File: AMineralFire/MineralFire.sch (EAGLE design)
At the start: 77 parts, among them IC1 LM358, IC2 OP-AMP, Q1 20MHz, Q2 20MHz, Q3 2N3906, Q4 2N3906, Q5 2N3906, Q6 2N3906, Q7 2N3906, Q8 2N3906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

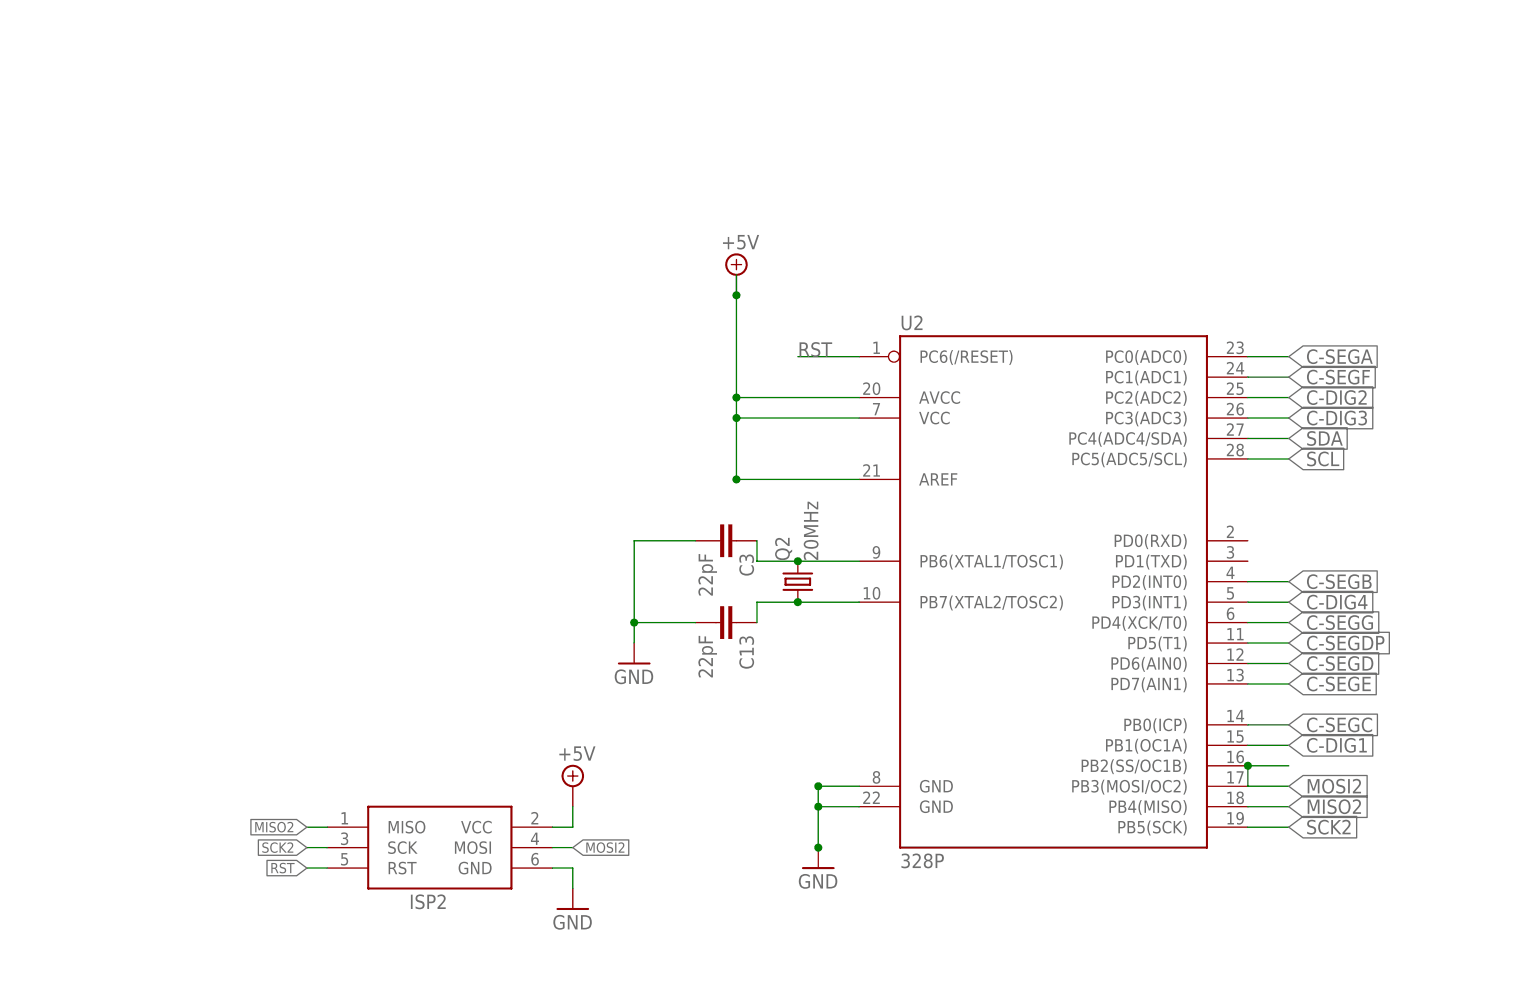
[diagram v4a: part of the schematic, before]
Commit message: Moving atmega to smd
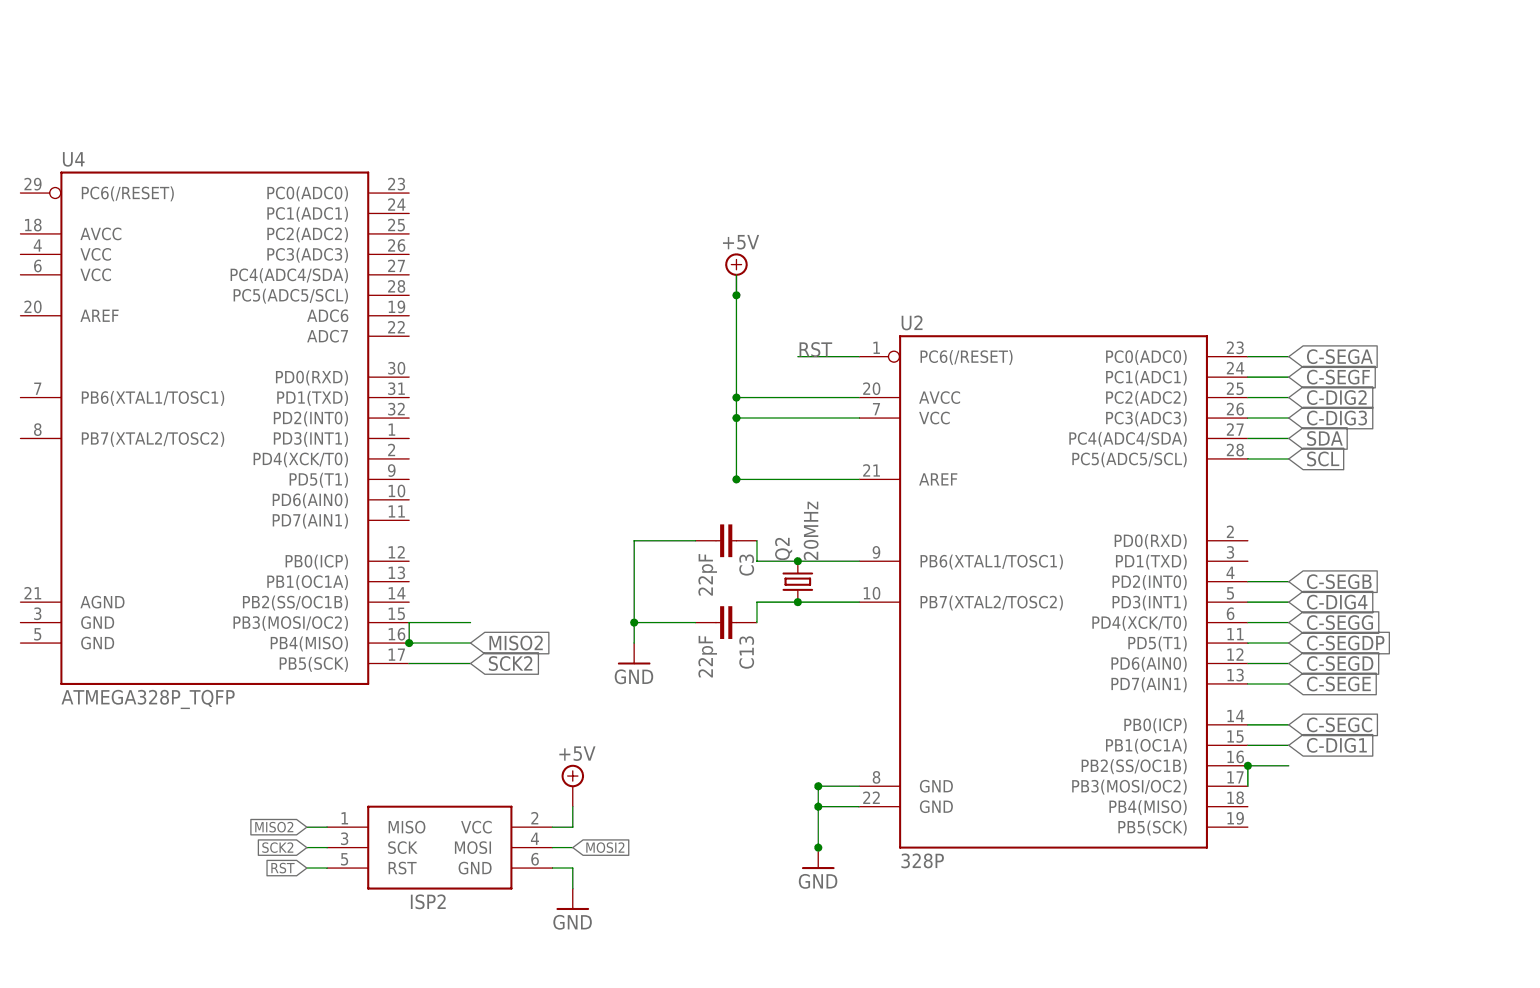
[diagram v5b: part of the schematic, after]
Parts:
- added U4: ATMEGA328P_TQFP, SparkFun-IC-Microcontroller:ATMEGA328P_TQFP
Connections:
- net MISO2: now also U4.PB3(MOSI/OC2), U4.PB4(MISO); no longer U2.PB4(MISO)
- net SCK2: now also U4.PB5(SCK); no longer U2.PB5(SCK)

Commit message: moving to SMD
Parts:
- removed C1, C2: 22pF, SparkFun-Capacitors:22PF-0603-50V-5%
- removed IC1: LM358, SparkFun-IC-Amplifiers:LM358
- removed Q1: 20MHz, adafruit:CRYSTALHC49UP
- removed U1, U2: 328P, SparkFun-IC-Microcontroller:ATMEGA328P_PDIP
- removed V1: 7432N, 74ttl-din:7432N
- added C14, C15: 22pF, SparkFun-Capacitors:22PF-0603-50V-5%
- added IC3: 7432D, 74xx-us:7432D
- added Q10: 20MHz, adafruit:CRYSTALHC49UP
- added U5: ATMEGA328P_TQFP, SparkFun-IC-Microcontroller:ATMEGA328P_TQFP
- C6: device rcl:C-EU075-032X103 -> rcl:C-EU01005
- D1, D2: value 200mA/100V/1V -> 250mA/100V; device SparkFun-DiscreteSemi:DIODE-1N4148 -> SparkFun-DiscreteSemi:DIODE-BAS16J
- Q3, Q4, Q5, Q6, Q7, Q8, Q9: value 2N3906 -> 200mA/40V; device transistor-pnp:2N3906 -> SparkFun-DiscreteSemi:TRANS_PNP-PMBT3906|MMBT3906L
- R5: device SparkFun-Resistors:100KOHM-HORIZ-1/4W-5% -> SparkFun-Resistors:100KOHM-0603-1/10W-1%
- R9: device SparkFun-Resistors:10KOHM-HORIZ-1/4W-1% -> SparkFun-Resistors:10KOHM-0603-1/10W-1%
- T1, T2, T3, T4, T5: value 200mA/40V -> 600mA/40V; device SparkFun-DiscreteSemi:TRANS_NPN-2N3904 -> SparkFun-DiscreteSemi:TRANS_NPN-MMBT2222AL
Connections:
- removed net CS: U1.PB2(SS/OC1B)
- removed net N$1: C1.1, Q1.2, U1.PB6(XTAL1/TOSC1)
- removed net N$2: C2.1, Q1.1, U1.PB7(XTAL2/TOSC2)
- new net N$21: C14.1, Q10.2, U5.PB6(XTAL1/TOSC1)
- new net N$22: C15.1, Q10.1, U5.PB7(XTAL2/TOSC2)
- new net RST2: ISP2.RST, U4.PC6(/RESET)
- net +12V: now also IC2G3.P$V+; no longer IC1G3.P$V+
- net +5V: now also IC3P.VCC, U4.AREF, U4.AVCC, U4.VCC@4, U4.VCC@6, U5.AREF, U5.AVCC, U5.VCC@4, U5.VCC@6; no longer U1.AREF, U1.AVCC, U1.VCC, U2.AREF, U2.AVCC, U2.VCC, V1/+UB.+UB
- net B_TRIG: now also U5.PD3(INT1); no longer U1.PD3(INT1)
- net C-DIG1: now also U4.PB1(OC1A); no longer U2.PB1(OC1A)
- net C-DIG2: now also U4.PC2(ADC2); no longer U2.PC2(ADC2)
- net C-DIG3: now also U4.PC3(ADC3); no longer U2.PC3(ADC3)
- net C-DIG4: now also U4.PD3(INT1); no longer U2.PD3(INT1)
- net C-SEGA: now also U4.PC0(ADC0); no longer U2.PC0(ADC0)
- net C-SEGB: now also U4.PD2(INT0); no longer U2.PD2(INT0)
- net C-SEGC: now also U4.PB0(ICP); no longer U2.PB0(ICP)
- net C-SEGD: now also U4.PD6(AIN0); no longer U2.PD6(AIN0)
- net C-SEGDP: now also U4.PD5(T1); no longer U2.PD5(T1)
- net C-SEGE: now also U4.PD7(AIN1); no longer U2.PD7(AIN1)
- net C-SEGF: now also U4.PC1(ADC1); no longer U2.PC1(ADC1)
- net C-SEGG: now also U4.PD4(XCK/T0); no longer U2.PD4(XCK/T0)
- net GND: now also C14.2, C15.2, IC3P.GND, U4.AGND, U4.GND@3, U4.GND@5, U5.AGND, U5.GND@3, U5.GND@5; no longer C1.2, C2.2, IC1G3.P$V-, U1.GND@1, U1.GND@2, U2.GND@1, U2.GND@2, V1/-UB.-UB
- net LBUTTON: now also IC3A.I1; no longer V1/1.B
- net LTRIG: now also IC3A.I0; no longer V1/1.A
- net MISO: now also U5.PB4(MISO); no longer U1.PB4(MISO)
- net MISO2: no longer U4.PB3(MOSI/OC2)
- net MOSI: now also U5.PB3(MOSI/OC2); no longer U1.PB3(MOSI/OC2)
- net MOSI2: now also U4.PB3(MOSI/OC2); no longer U2.PB2(SS/OC1B), U2.PB3(MOSI/OC2)
- net N$7: now also U4.PB6(XTAL1/TOSC1); no longer U2.PB6(XTAL1/TOSC1)
- net N$8: now also U4.PB7(XTAL2/TOSC2); no longer U2.PB7(XTAL2/TOSC2)
- net RST: now also U5.PC6(/RESET); no longer ISP2.RST, U1.PC6(/RESET), U2.PC6(/RESET)
- net SCK: now also U5.PB5(SCK); no longer U1.PB5(SCK)
- net SCL: now also U4.PC5(ADC5/SCL), U5.PC5(ADC5/SCL); no longer U1.PC5(ADC5/SCL), U2.PC5(ADC5/SCL)
- net SDA: now also U4.PC4(ADC4/SDA), U5.PC4(ADC4/SDA); no longer U1.PC4(ADC4/SDA), U2.PC4(ADC4/SDA)
- net T1: now also U5.PD5(T1); no longer U1.PD5(T1)
- net T2: now also U5.PD4(XCK/T0); no longer U1.PD4(XCK/T0)
- net T3: now also U5.PC2(ADC2); no longer U1.PC2(ADC2)
- net T4: now also U5.PC3(ADC3); no longer U1.PC3(ADC3)
- net T5: now also U5.PC0(ADC0); no longer U1.PC0(ADC0)
- net T6: now also U5.PC1(ADC1); no longer U1.PC1(ADC1)
- net T7: now also U5.PD6(AIN0); no longer U1.PD6(AIN0)
- net T8: now also U5.PD7(AIN1); no longer U1.PD7(AIN1)
- net TRIG: now also IC3A.O, U5.PD2(INT0); no longer U1.PD2(INT0), V1/1.Y
- net TRIGO: now also U5.PB0(ICP); no longer U1.PB0(ICP)
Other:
- moved on the sheet: C13, C3, ISP2, Q2, U4
